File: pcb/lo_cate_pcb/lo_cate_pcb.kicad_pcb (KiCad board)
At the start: 4 copper layers, 100 x 50 mm, 58 parts, among them J1 Conn_01x07_Pin, J2 690-005-299-043, SW1 MICRO_RESET, SW2 MICRO_ON, SW3 BUTTON1, SW4 BUTTON2, SW5 BUTTON3, U1 STM32F401RETx, U2 BMI323, U3 LED1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

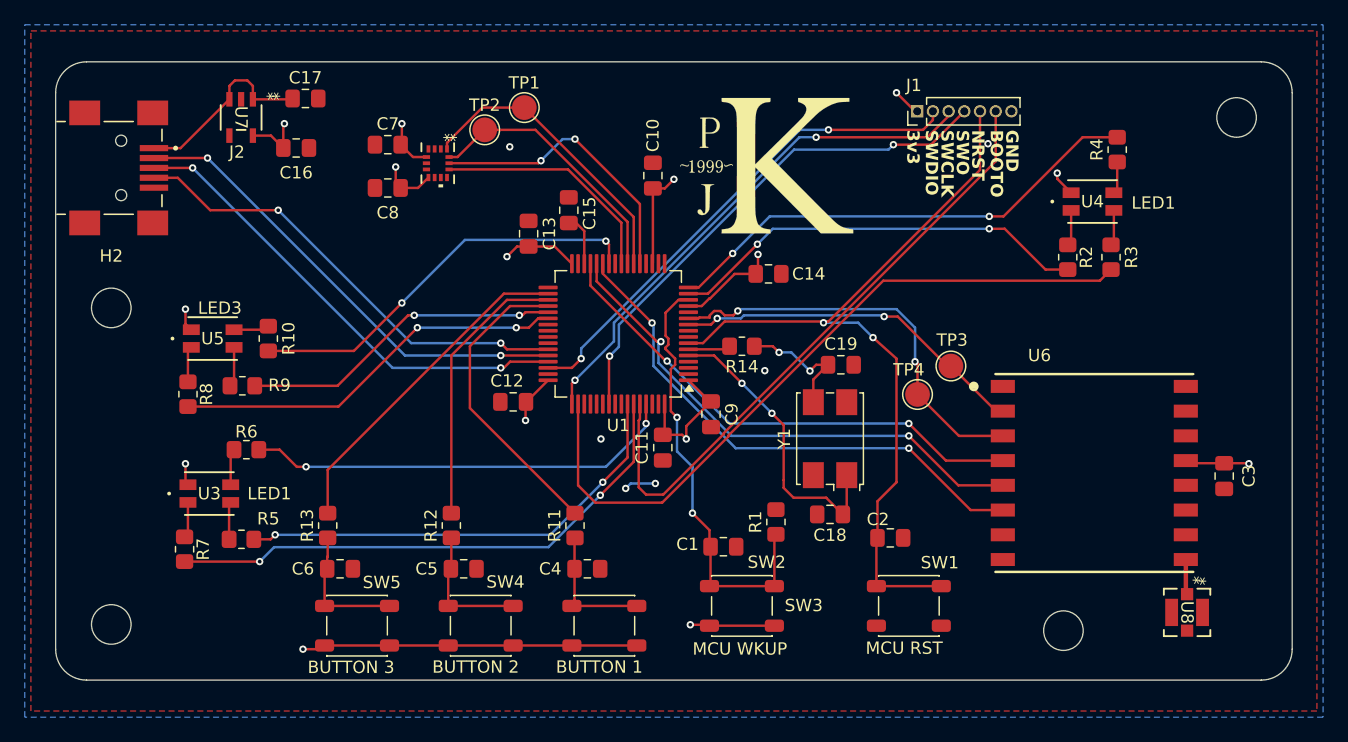
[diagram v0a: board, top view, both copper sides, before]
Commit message: broke a usart to header pins
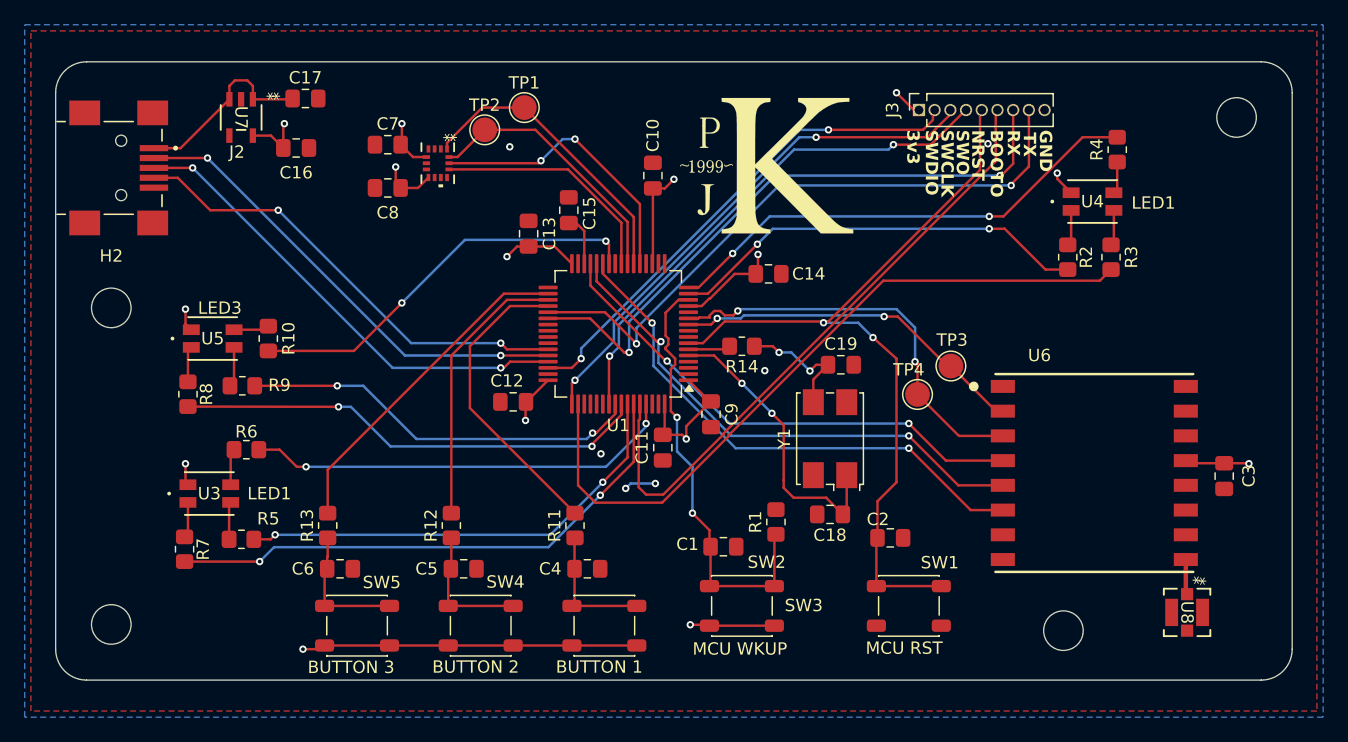
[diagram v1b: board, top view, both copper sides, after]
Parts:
- removed J1: Conn_01x07_Pin, Connector_PinHeader_1.27mm:PinHeader_1x07_P1.27mm_Vertical
- added J3: Conn_01x09_Pin, Connector_PinSocket_1.27mm:PinSocket_1x09_P1.27mm_Vertical, F.Cu at (167.3, 77.5)
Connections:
- U1 pad 37: /LED3_RED -> /UART_TX
- U1 pad 38: /LED3_BLUE -> /UART_RX
- U1 pad 56: unconnected-(U1-PB4-Pad56) -> /LED3_RED
- U1 pad 57: unconnected-(U1-PB5-Pad57) -> /LED3_BLUE
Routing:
- net /UART_TX: track 0.00 -> 51.6 mm, vias 0 -> 2
- net /UART_RX: track 0.00 -> 51.1 mm, vias 0 -> 2
- net /LED3_BLUE: track 32.1 -> 38.6 mm
- net /LED3_RED: track 26.2 -> 32.6 mm
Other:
- board text added: "RX"
- board text added: "TX"

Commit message: Submitted PCB for manufactoring
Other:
- board text added: "290624"
- board text added: "LO-CATE V1"
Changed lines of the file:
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@@
 			(plot_on_all_layers_selection 0x0000000_00000000)
 			(disableapertmacros no)
-			(usegerberextensions no)
+			(usegerberextensions yes)
 			(usegerberattributes yes)
 			(usegerberadvancedattributes yes)
-			(creategerberjobfile yes)
+			(creategerberjobfile no)
 			(dashed_line_dash_ratio 12.000000)
 			(dashed_line_gap_ratio 3.000000)
@@
 			(plotinvisibletext no)
 			(sketchpadsonfab no)
-			(subtractmaskfromsilk no)
+			(subtractmaskfromsilk yes)
 			(outputformat 1)
 			(mirror no)
-			(drillshape 1)
+			(drillshape 0)
 			(scaleselection 1)
-			(outputdirectory "")
+			(outputdirectory "manf-files/")
 		)
 	)
@@
 		)
 	)
+	(gr_text "290624"
+		(at 106.4 120.5 0)
+		(layer "F.SilkS")
+		(effects
+			(font
+				(size 1 1)
+				(thickness 0.1)
+			)
+			(justify left bottom)
+		)
+	)
 	(gr_text "SWDIO\n"
 		(at 167.775 79.1 270)
@@
 			)
 			(justify left bottom)
+		)
+	)
+	(gr_text "LO-CATE V1\n"
+		(at 106.6 118.9 0)
+		(layer "F.SilkS")
+		(effects
+			(font
+				(size 1 1)
+				(thickness 0.2)
+				(bold yes)
+			)
+			(justify left bottom)
